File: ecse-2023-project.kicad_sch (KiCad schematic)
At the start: 11 parts, among them J1 Screw_Terminal_01x02, J2 Screw_Terminal_01x02, J3 Screw_Terminal_01x02, J4 Screw_Terminal_01x03, J5 Conn_01x03_Female, Q1 IRF740, Q2 IRF740, U1 ESP32_DevKit_V1_DOIT

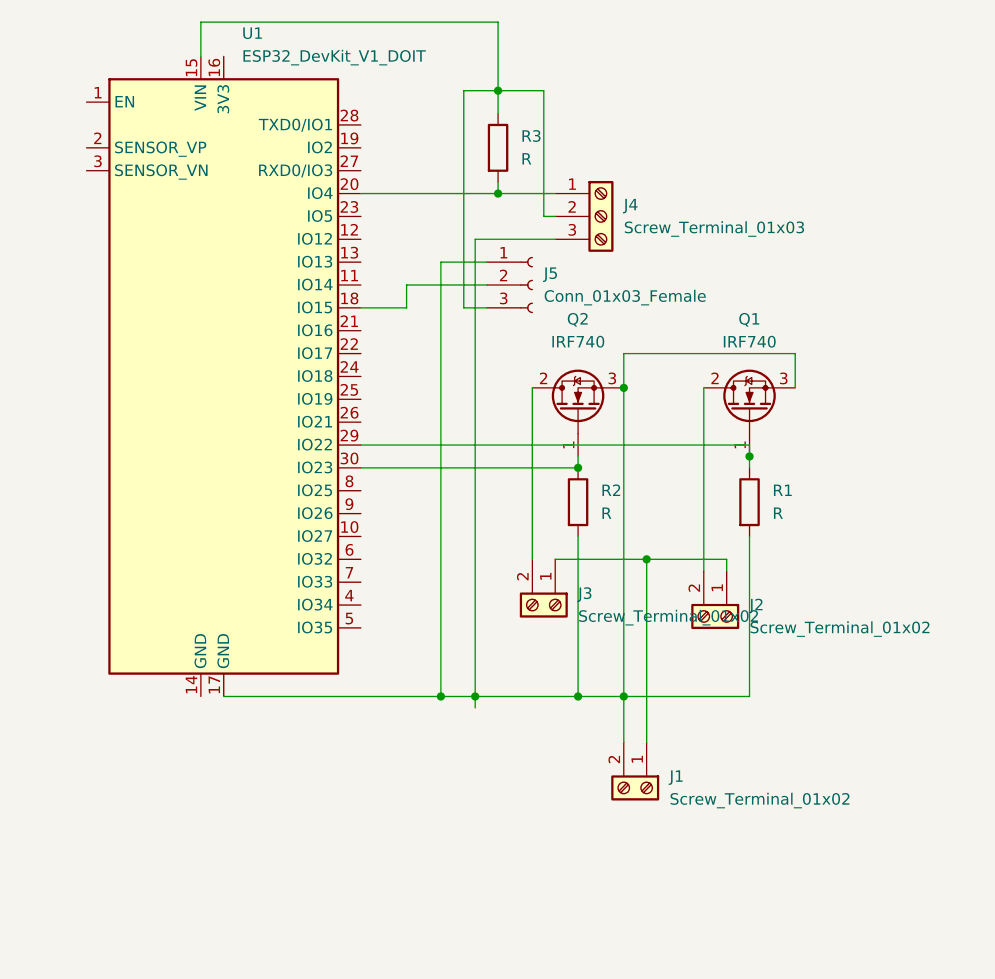
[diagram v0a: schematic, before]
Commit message: replaced screw terminal with barrel jack for the power in port. changed label from 12v to power in. changed pin order for temp port to match label
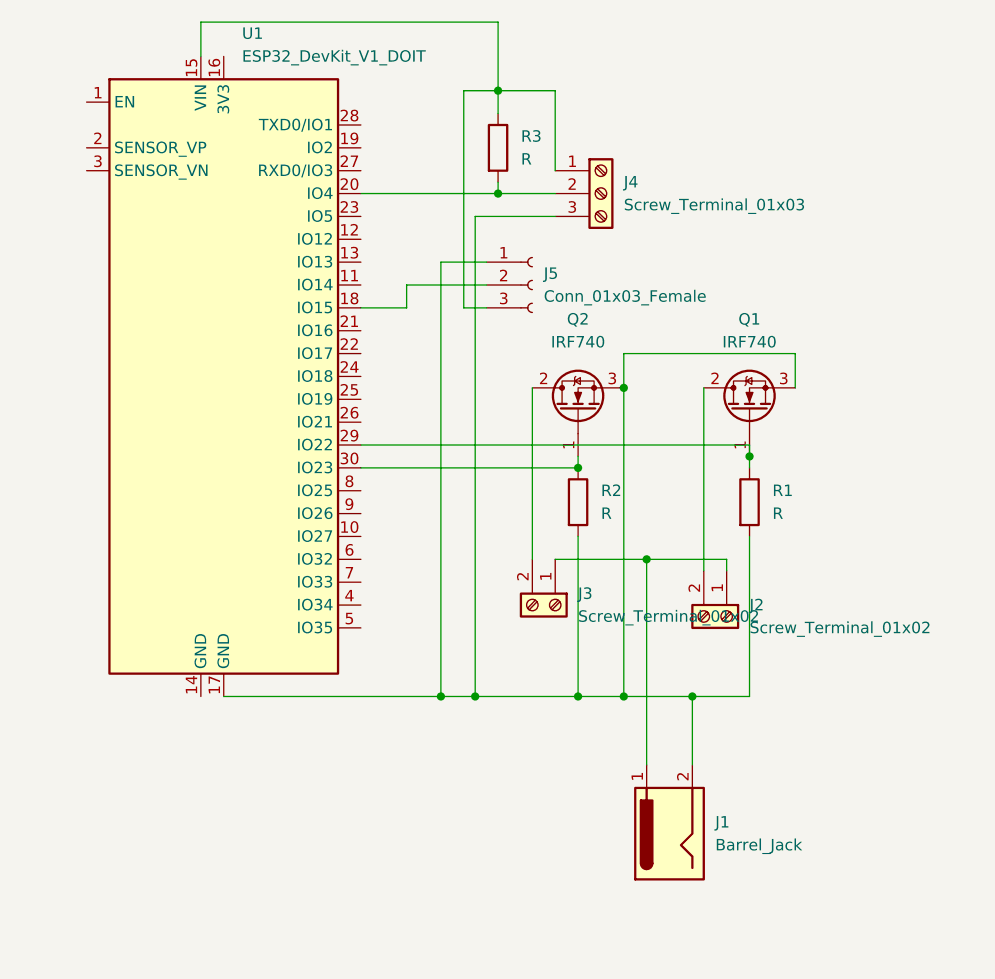
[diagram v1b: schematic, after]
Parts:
- removed J1: Screw_Terminal_01x02, TerminalBlock_Phoenix:TerminalBlock_Phoenix_MKDS-1,5-2_1x02_P5.00mm_Horizontal, symbol Connector:Screw_Terminal_01x02
- added J1: Barrel_Jack, Connector_BarrelJack:BarrelJack_Horizontal, symbol Connector:Barrel_Jack
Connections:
- net at J4.3 (Pin_3), J5.1 (Pin_1), Q1.3 (S)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: now also J1.2
- net at J2.1 (Pin_1), J3.1 (Pin_1): now also J1.1
- net at J5.3 (Pin_3), R3.1, U1.15 (VIN): now also J4.1 (Pin_1); no longer J4.2 (Pin_2)
- net at R3.2, U1.20 (IO4): now also J4.2 (Pin_2); no longer J4.1 (Pin_1)
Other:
- moved on the sheet: J4
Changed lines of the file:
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@@
 (kicad_sch (version 20211123) (generator eeschema)
   (paper "A4")
+  (junction (at 168.91 129.54) (diameter 0) (color 0 0 0 0)
+  )
   (junction (at 140.97 129.54) (diameter 0) (color 0 0 0 0)
   )
@@
   (junction (at 156.21 129.54) (diameter 0) (color 0 0 0 0)
   )
+  (junction (at 147.32 73.66) (diameter 0) (color 0 0 0 0)
+  )
   (junction (at 161.29 95.25) (diameter 0) (color 0 0 0 0)
   )
   (junction (at 144.78 129.54) (diameter 0) (color 0 0 0 0)
   )
-  (junction (at 147.32 73.66) (diameter 0) (color 0 0 0 0)
-  )
   (wire (pts (xy 140.97 129.54) (xy 144.78 129.54))
     (stroke (width 0) (type default) (color 0 0 0 0))
   )
-  (wire (pts (xy 144.78 78.74) (xy 144.78 129.54))
+  (wire (pts (xy 144.78 76.2) (xy 144.78 129.54))
     (stroke (width 0) (type default) (color 0 0 0 0))
   )
@@
     (stroke (width 0) (type default) (color 0 0 0 0))
   )
-  (wire (pts (xy 144.78 130.81) (xy 144.78 129.54))
-    (stroke (width 0) (type default) (color 0 0 0 0))
-  )
   (wire (pts (xy 175.26 129.54) (xy 175.26 111.76))
     (stroke (width 0) (type default) (color 0 0 0 0))
@@
     (stroke (width 0) (type default) (color 0 0 0 0))
   )
+  (wire (pts (xy 153.67 62.23) (xy 153.67 71.12))
+    (stroke (width 0) (type default) (color 0 0 0 0))
+  )
   (wire (pts (xy 143.51 86.36) (xy 143.51 62.23))
     (stroke (width 0) (type default) (color 0 0 0 0))
@@
     (stroke (width 0) (type default) (color 0 0 0 0))
   )
-  (wire (pts (xy 161.29 129.54) (xy 161.29 134.62))
-    (stroke (width 0) (type default) (color 0 0 0 0))
-  )
   (wire (pts (xy 114.3 58.42) (xy 114.3 54.61))
     (stroke (width 0) (type default) (color 0 0 0 0))
   )
+  (wire (pts (xy 147.32 73.66) (xy 153.67 73.66))
+    (stroke (width 0) (type default) (color 0 0 0 0))
+  )
   (wire (pts (xy 153.67 114.3) (xy 163.83 114.3))
     (stroke (width 0) (type default) (color 0 0 0 0))
@@
     (stroke (width 0) (type default) (color 0 0 0 0))
   )
-  (wire (pts (xy 153.67 78.74) (xy 144.78 78.74))
-    (stroke (width 0) (type default) (color 0 0 0 0))
-  )
   (wire (pts (xy 132.08 104.14) (xy 156.21 104.14))
     (stroke (width 0) (type default) (color 0 0 0 0))
@@
     (stroke (width 0) (type default) (color 0 0 0 0))
   )
-  (wire (pts (xy 153.67 76.2) (xy 152.4 76.2))
-    (stroke (width 0) (type default) (color 0 0 0 0))
-  )
-  (wire (pts (xy 152.4 76.2) (xy 152.4 62.23))
+  (wire (pts (xy 168.91 129.54) (xy 175.26 129.54))
     (stroke (width 0) (type default) (color 0 0 0 0))
   )
@@
     (stroke (width 0) (type default) (color 0 0 0 0))
   )
-  (wire (pts (xy 152.4 62.23) (xy 147.32 62.23))
-    (stroke (width 0) (type default) (color 0 0 0 0))
-  )
   (wire (pts (xy 151.13 95.25) (xy 151.13 114.3))
     (stroke (width 0) (type default) (color 0 0 0 0))
   )
-  (wire (pts (xy 163.83 114.3) (xy 163.83 134.62))
+  (wire (pts (xy 163.83 114.3) (xy 163.83 137.16))
     (stroke (width 0) (type default) (color 0 0 0 0))
   )
@@
     (stroke (width 0) (type default) (color 0 0 0 0))
   )
-  (wire (pts (xy 147.32 73.66) (xy 153.67 73.66))
-    (stroke (width 0) (type default) (color 0 0 0 0))
-  )
   (wire (pts (xy 175.26 104.14) (xy 175.26 102.87))
     (stroke (width 0) (type default) (color 0 0 0 0))
@@
     (stroke (width 0) (type default) (color 0 0 0 0))
   )
+  (wire (pts (xy 153.67 76.2) (xy 144.78 76.2))
+    (stroke (width 0) (type default) (color 0 0 0 0))
+  )
+  (wire (pts (xy 147.32 62.23) (xy 153.67 62.23))
+    (stroke (width 0) (type default) (color 0 0 0 0))
+  )
   (wire (pts (xy 156.21 111.76) (xy 156.21 129.54))
     (stroke (width 0) (type default) (color 0 0 0 0))
@@
     (stroke (width 0) (type default) (color 0 0 0 0))
   )
-  (wire (pts (xy 161.29 129.54) (xy 175.26 129.54))
+  (wire (pts (xy 161.29 129.54) (xy 168.91 129.54))
+    (stroke (width 0) (type default) (color 0 0 0 0))
+  )
+  (wire (pts (xy 168.91 129.54) (xy 168.91 137.16))
     (stroke (width 0) (type default) (color 0 0 0 0))
   )
@@
     (pin "2")
   )
-  (symbol (lib_id "Connector:Screw_Terminal_01x02") (at 163.83 139.7 270) (unit 1)
-    (in_bom yes) (on_board yes) (fields_autoplaced)
-    (property "Reference" "J1" (id 0) (at 166.37 138.4299 90)
-      (effects (font (size 1.27 1.27)) (justify left))
-    )
-    (property "Value" "Screw_Terminal_01x02" (id 1) (at 166.37 140.9699 90)
-      (effects (font (size 1.27 1.27)) (justify left))
-    )
-    (property "Footprint" "TerminalBlock_Phoenix:TerminalBlock_Phoenix_MKDS-1,5-2_1x02_P5.00mm_Horizontal" (id 2) (at 163.83 139.7 0)
-      (effects (font (size 1.27 1.27)) hide)
-    )
-    (property "Datasheet" "~" (id 3) (at 163.83 139.7 0)
-      (effects (font (size 1.27 1.27)) hide)
-    )
-    (pin "1")
-    (pin "2")
-  )
-  (symbol (lib_id "Connector:Screw_Terminal_01x03") (at 158.75 76.2 0) (unit 1)
-    (in_bom yes) (on_board yes) (fields_autoplaced)
-    (property "Reference" "J4" (id 0) (at 161.29 74.9299 0)
-      (effects (font (size 1.27 1.27)) (justify left))
-    )
-    (property "Value" "Screw_Terminal_01x03" (id 1) (at 161.29 77.4699 0)
-      (effects (font (size 1.27 1.27)) (justify left))
-    )
-    (property "Footprint" "TerminalBlock_Phoenix:TerminalBlock_Phoenix_MKDS-1,5-3_1x03_P5.00mm_Horizontal" (id 2) (at 158.75 76.2 0)
-      (effects (font (size 1.27 1.27)) hide)
-    )
-    (property "Datasheet" "~" (id 3) (at 158.75 76.2 0)
+  (symbol (lib_id "Connector:Screw_Terminal_01x03") (at 158.75 73.66 0) (unit 1)
+    (in_bom yes) (on_board yes) (fields_autoplaced)
+    (property "Reference" "J4" (id 0) (at 161.29 72.3899 0)
+      (effects (font (size 1.27 1.27)) (justify left))
+    )
+    (property "Value" "Screw_Terminal_01x03" (id 1) (at 161.29 74.9299 0)
+      (effects (font (size 1.27 1.27)) (justify left))
+    )
+    (property "Footprint" "TerminalBlock_Phoenix:TerminalBlock_Phoenix_MKDS-1,5-3_1x03_P5.00mm_Horizontal" (id 2) (at 158.75 73.66 0)
+      (effects (font (size 1.27 1.27)) hide)
+    )
+    (property "Datasheet" "~" (id 3) (at 158.75 73.66 0)
       (effects (font (size 1.27 1.27)) hide)
     )
@@
     (pin "9")
   )
+  (symbol (lib_id "Connector:Barrel_Jack") (at 166.37 144.78 90) (unit 1)
+    (in_bom yes) (on_board yes) (fields_autoplaced)
+    (property "Reference" "J1" (id 0) (at 171.45 143.5099 90)
+      (effects (font (size 1.27 1.27)) (justify right))
+    )
+    (property "Value" "Barrel_Jack" (id 1) (at 171.45 146.0499 90)
+      (effects (font (size 1.27 1.27)) (justify right))
+    )
+    (property "Footprint" "Connector_BarrelJack:BarrelJack_Horizontal" (id 2) (at 167.386 143.51 0)
+      (effects (font (size 1.27 1.27)) hide)
+    )
+    (property "Datasheet" "~" (id 3) (at 167.386 143.51 0)
+      (effects (font (size 1.27 1.27)) hide)
+    )
+    (pin "1")
+    (pin "2")
+  )
   (symbol (lib_id "Connector:Screw_Terminal_01x02") (at 172.72 120.65 270) (unit 1)
     (in_bom yes) (on_board yes) (fields_autoplaced)
@@
   )
   (symbol_instances
-    (path "/3411fe21-0c4c-48bc-88d3-2a677c9482dc"
-      (reference "J1") (unit 1) (value "Screw_Terminal_01x02") (footprint "TerminalBlock_Phoenix:TerminalBlock_Phoenix_MKDS-1,5-2_1x02_P5.00mm_Horizontal")
+    (path "/6ba60c75-a0be-4d07-af0a-ecf96993ef28"
+      (reference "J1") (unit 1) (value "Barrel_Jack") (footprint "Connector_BarrelJack:BarrelJack_Horizontal")
     )
     (path "/7ef3817d-5874-4567-9ee9-303975f373b8"

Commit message: added a buck to the pcb so that that prower port can power the esp
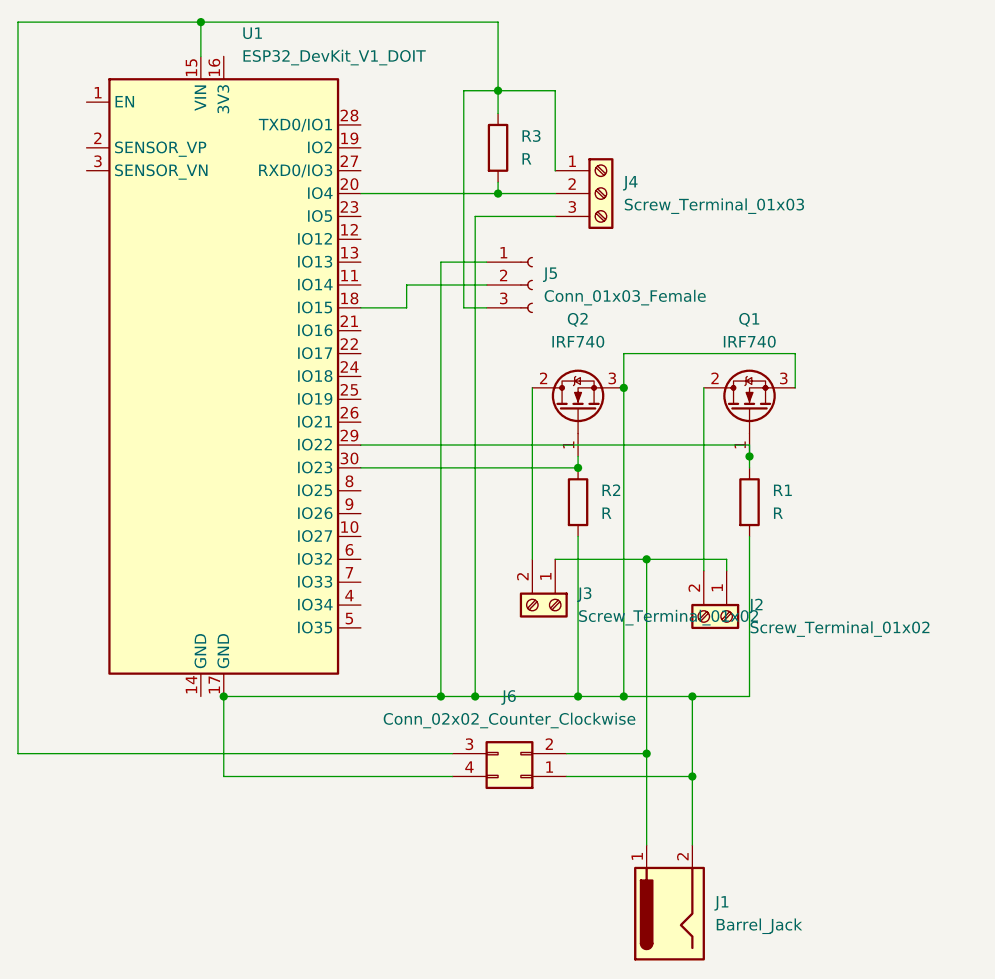
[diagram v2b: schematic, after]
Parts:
- added J6: Conn_02x02_Counter_Clockwise, Library:SRT_MPT1584EN_Module, symbol Connector_Generic:Conn_02x02_Counter_Clockwise
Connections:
- net at J1.2, J4.3 (Pin_3), J5.1 (Pin_1)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: now also J6.1 (Pin_1), J6.4 (Pin_4)
- net at J1.1, J2.1 (Pin_1), J3.1 (Pin_1): now also J6.2 (Pin_2)
- net at J4.1 (Pin_1), J5.3 (Pin_3), R3.1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: now also J6.3 (Pin_3)
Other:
- moved on the sheet: J1

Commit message: added optional buck converter for esp
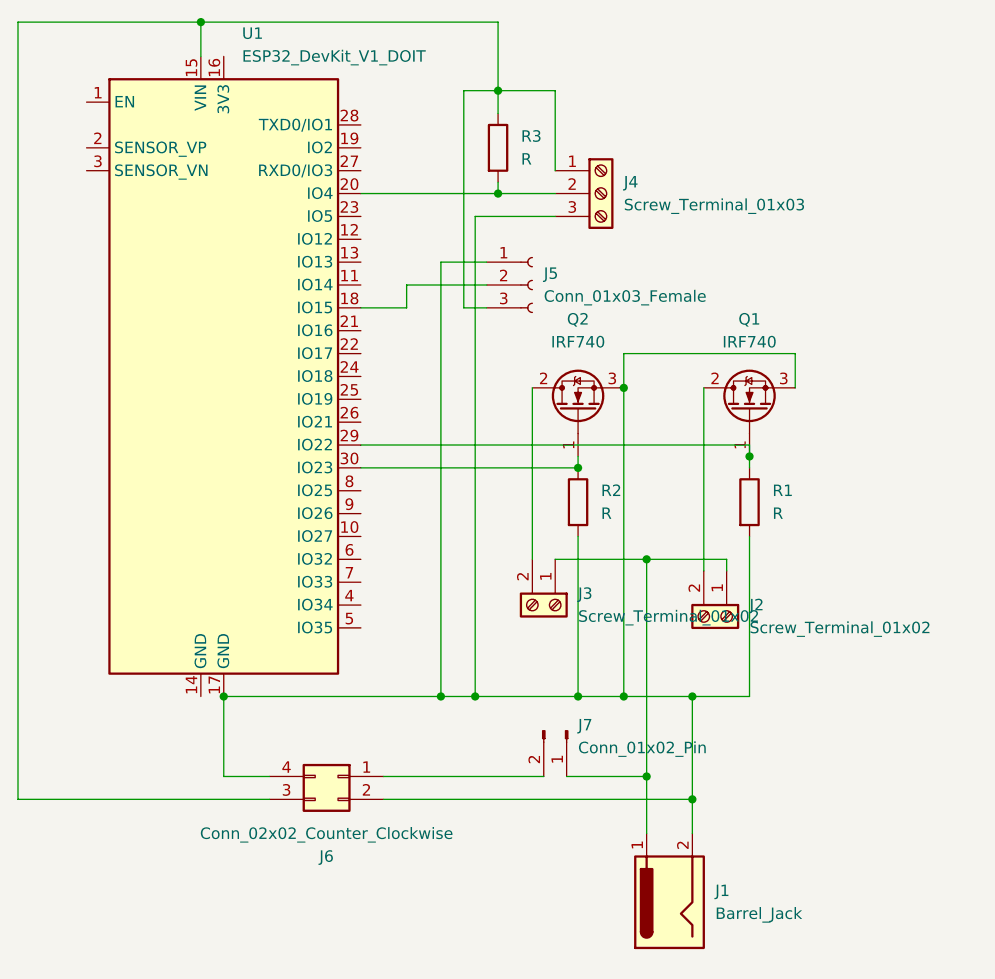
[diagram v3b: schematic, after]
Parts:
- added J7: Conn_01x02_Pin, Connector_PinHeader_2.54mm:PinHeader_1x02_P2.54mm_Vertical, symbol Connector:Conn_01x02_Pin
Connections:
- net at J1.2, J4.3 (Pin_3), J5.1 (Pin_1)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: now also J6.2 (Pin_2); no longer J6.1 (Pin_1)
- net at J1.1, J2.1 (Pin_1), J3.1 (Pin_1): now also J7.1 (Pin_1); no longer J6.2 (Pin_2)
- new net: J6.1 (Pin_1), J7.2 (Pin_2)
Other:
- moved on the sheet: J1, J6
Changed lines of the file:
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@@
 	)
 	(junction
-		(at 168.91 138.43)
+		(at 168.91 140.97)
 		(diameter 0)
 		(color 0 0 0 0)
@@
 	)
 	(junction
-		(at 163.83 135.89)
-		(diameter 0)
-		(color 0 0 0 0)
-	)
-	(junction
 		(at 163.83 114.3)
 		(diameter 0)
@@
 	)
 	(junction
+		(at 163.83 138.43)
+		(diameter 0)
+		(color 0 0 0 0)
+	)
+	(junction
 		(at 156.21 129.54)
 		(diameter 0)
@@
 	(wire
 		(pts
-			(xy 93.98 135.89) (xy 93.98 54.61)
+			(xy 116.84 138.43) (xy 121.92 138.43)
 		)
 		(stroke
@@
 	(wire
 		(pts
+			(xy 134.62 140.97) (xy 168.91 140.97)
+		)
+		(stroke
+			(width 0)
+			(type default)
+		)
+	)
+	(wire
+		(pts
 			(xy 144.78 76.2) (xy 144.78 129.54)
 		)
@@
 	(wire
 		(pts
-			(xy 163.83 135.89) (xy 163.83 146.05)
+			(xy 163.83 114.3) (xy 163.83 138.43)
+		)
+		(stroke
+			(width 0)
+			(type default)
+		)
+	)
+	(wire
+		(pts
+			(xy 163.83 138.43) (xy 163.83 144.78)
 		)
 		(stroke
@@
 	(wire
 		(pts
+			(xy 154.94 138.43) (xy 163.83 138.43)
+		)
+		(stroke
+			(width 0)
+			(type default)
+		)
+	)
+	(wire
+		(pts
 			(xy 161.29 91.44) (xy 180.34 91.44)
 		)
@@
 	(wire
 		(pts
-			(xy 142.24 138.43) (xy 116.84 138.43)
-		)
-		(stroke
-			(width 0)
-			(type default)
-		)
-	)
-	(wire
-		(pts
-			(xy 154.94 135.89) (xy 163.83 135.89)
-		)
-		(stroke
-			(width 0)
-			(type default)
-		)
-	)
-	(wire
-		(pts
 			(xy 116.84 129.54) (xy 140.97 129.54)
 		)
@@
 	(wire
 		(pts
-			(xy 163.83 114.3) (xy 163.83 135.89)
-		)
-		(stroke
-			(width 0)
-			(type default)
-		)
-	)
-	(wire
-		(pts
 			(xy 146.05 81.28) (xy 140.97 81.28)
 		)
@@
 	(wire
 		(pts
-			(xy 168.91 138.43) (xy 168.91 146.05)
+			(xy 93.98 54.61) (xy 93.98 140.97)
 		)
 		(stroke
@@
 	(wire
 		(pts
+			(xy 168.91 140.97) (xy 168.91 144.78)
+		)
+		(stroke
+			(width 0)
+			(type default)
+		)
+	)
+	(wire
+		(pts
 			(xy 147.32 62.23) (xy 153.67 62.23)
 		)
@@
 	(wire
 		(pts
+			(xy 134.62 138.43) (xy 152.4 138.43)
+		)
+		(stroke
+			(width 0)
+			(type default)
+		)
+	)
+	(wire
+		(pts
 			(xy 180.34 91.44) (xy 180.34 95.25)
 		)
@@
 	(wire
 		(pts
-			(xy 93.98 135.89) (xy 142.24 135.89)
-		)
-		(stroke
-			(width 0)
-			(type default)
-		)
-	)
-	(wire
-		(pts
 			(xy 161.29 129.54) (xy 168.91 129.54)
 		)
@@
 	(wire
 		(pts
-			(xy 168.91 129.54) (xy 168.91 138.43)
+			(xy 121.92 140.97) (xy 93.98 140.97)
+		)
+		(stroke
+			(width 0)
+			(type default)
+		)
+	)
+	(wire
+		(pts
+			(xy 168.91 129.54) (xy 168.91 140.97)
 		)
 		(stroke
@@
 		(pts
 			(xy 146.05 86.36) (xy 143.51 86.36)
-		)
-		(stroke
-			(width 0)
-			(type default)
-		)
-	)
-	(wire
-		(pts
-			(xy 154.94 138.43) (xy 168.91 138.43)
 		)
 		(stroke
@@
 	(symbol
 		(lib_id "Connector_Generic:Conn_02x02_Counter_Clockwise")
-		(at 149.86 138.43 180)
+		(at 129.54 138.43 0)
+		(mirror y)
 		(unit 1)
 		(exclude_from_sim no)
@@
 		(on_board yes)
 		(dnp no)
-		(fields_autoplaced yes)
 		(property "Reference" "J6"
-			(at 148.59 129.54 0)
+			(at 128.27 147.32 0)
 			(effects
 				(font
@@
 		)
 		(property "Value" "Conn_02x02_Counter_Clockwise"
-			(at 148.59 132.08 0)
+			(at 128.27 144.78 0)
 			(effects
 				(font
@@
 		)
 		(property "Footprint" "Library:SRT_MPT1584EN_Module"
-			(at 149.86 138.43 0)
+			(at 129.54 138.43 0)
 			(effects
 				(font
@@
 		)
 		(property "Datasheet" "~"
-			(at 149.86 138.43 0)
+			(at 129.54 138.43 0)
 			(effects
 				(font
@@
 		)
 		(property "Description" "Generic connector, double row, 02x02, counter clockwise pin numbering scheme (similar to DIP package numbering), script generated (kicad-library-utils/schlib/autogen/connector/)"
-			(at 149.86 138.43 0)
+			(at 129.54 138.43 0)
 			(effects
 				(font
@@
 	(symbol
 		(lib_id "Connector:Barrel_Jack")
-		(at 166.37 153.67 90)
+		(at 166.37 152.4 90)
 		(unit 1)
 		(exclude_from_sim no)
@@
 		(fields_autoplaced yes)
 		(property "Reference" "J1"
-			(at 171.45 152.3999 90)
+			(at 171.45 151.1299 90)
 			(effects
 				(font
@@
 		)
 		(property "Value" "Barrel_Jack"
-			(at 171.45 154.9399 90)
+			(at 171.45 153.6699 90)
 			(effects
 				(font
@@
 		)
 		(property "Footprint" "Connector_BarrelJack:BarrelJack_Horizontal"
-			(at 167.386 152.4 0)
+			(at 167.386 151.13 0)
 			(effects
 				(font
@@
 		)
 		(property "Datasheet" "~"
-			(at 167.386 152.4 0)
+			(at 167.386 151.13 0)
 			(effects
 				(font
@@
 		)
 		(property "Description" ""
-			(at 166.37 153.67 0)
+			(at 166.37 152.4 0)
 			(effects
 				(font
@@
 					(unit 1)
 				)
+			)
+		)
+	)
+	(symbol
+		(lib_id "Connector:Conn_01x02_Pin")
+		(at 154.94 133.35 270)
+		(unit 1)
+		(exclude_from_sim no)
+		(in_bom yes)
+		(on_board yes)
+		(dnp no)
+		(fields_autoplaced yes)
+		(property "Reference" "J7"
+			(at 156.21 132.7149 90)
+			(effects
+				(font
+					(size 1.27 1.27)
+				)
+				(justify left)
+			)
+		)
+		(property "Value" "Conn_01x02_Pin"
+			(at 156.21 135.2549 90)
+			(effects
+				(font
+					(size 1.27 1.27)
+				)
+				(justify left)
+			)
+		)
+		(property "Footprint" "Connector_PinHeader_2.54mm:PinHeader_1x02_P2.54mm_Vertical"
+			(at 154.94 133.35 0)
+			(effects
+				(font
+					(size 1.27 1.27)
+				)
+				(hide yes)
+			)
+		)
+		(property "Datasheet" "~"
+			(at 154.94 133.35 0)
+			(effects
+				(font
+					(size 1.27 1.27)
+				)
+				(hide yes)
+			)
+		)
+		(property "Description" "Generic connector, single row, 01x02, script generated"
+			(at 154.94 133.35 0)
+			(effects
+				(font
+					(size 1.27 1.27)
+				)
+				(hide yes)
+			)
+		)
+		(pin "1"
+		)
+		(pin "2"
+		)
+		(instances
+			(project "ecse-2023-project"
+				(path "/102f78f1-ce47-494a-952c-73291e6a29b8"
+					(reference "J7")
+					(unit 1)
+				)
